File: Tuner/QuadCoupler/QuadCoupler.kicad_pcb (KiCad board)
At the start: 2 copper layers, 100 x 100 mm, 89 parts, among them J1 Conn_01x02, J10 Conn_01x02, J2 Conn_Coaxial, J21 Conn_01x01, J22 Conn_01x01, J23 Conn_01x01, J24 Conn_01x01, J3 Conn_Coaxial, J4 Conn_Coaxial, J5 Conn_Coaxial, J6 Conn_Coaxial, J7 Conn_01x02, J8 Conn_01x02, J9 Conn_01x02

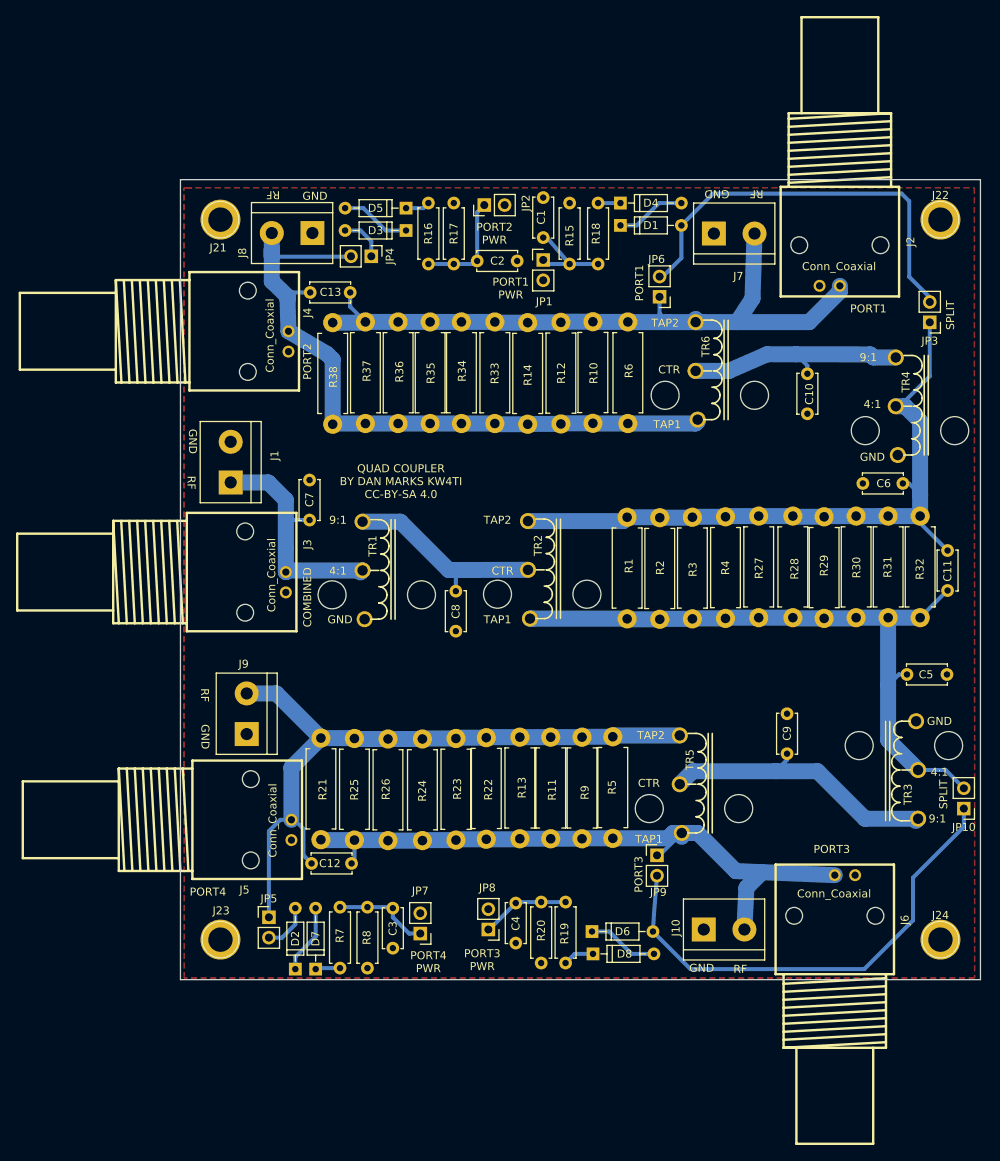
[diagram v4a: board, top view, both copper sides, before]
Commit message: Added BNC and screw terminal combo pads
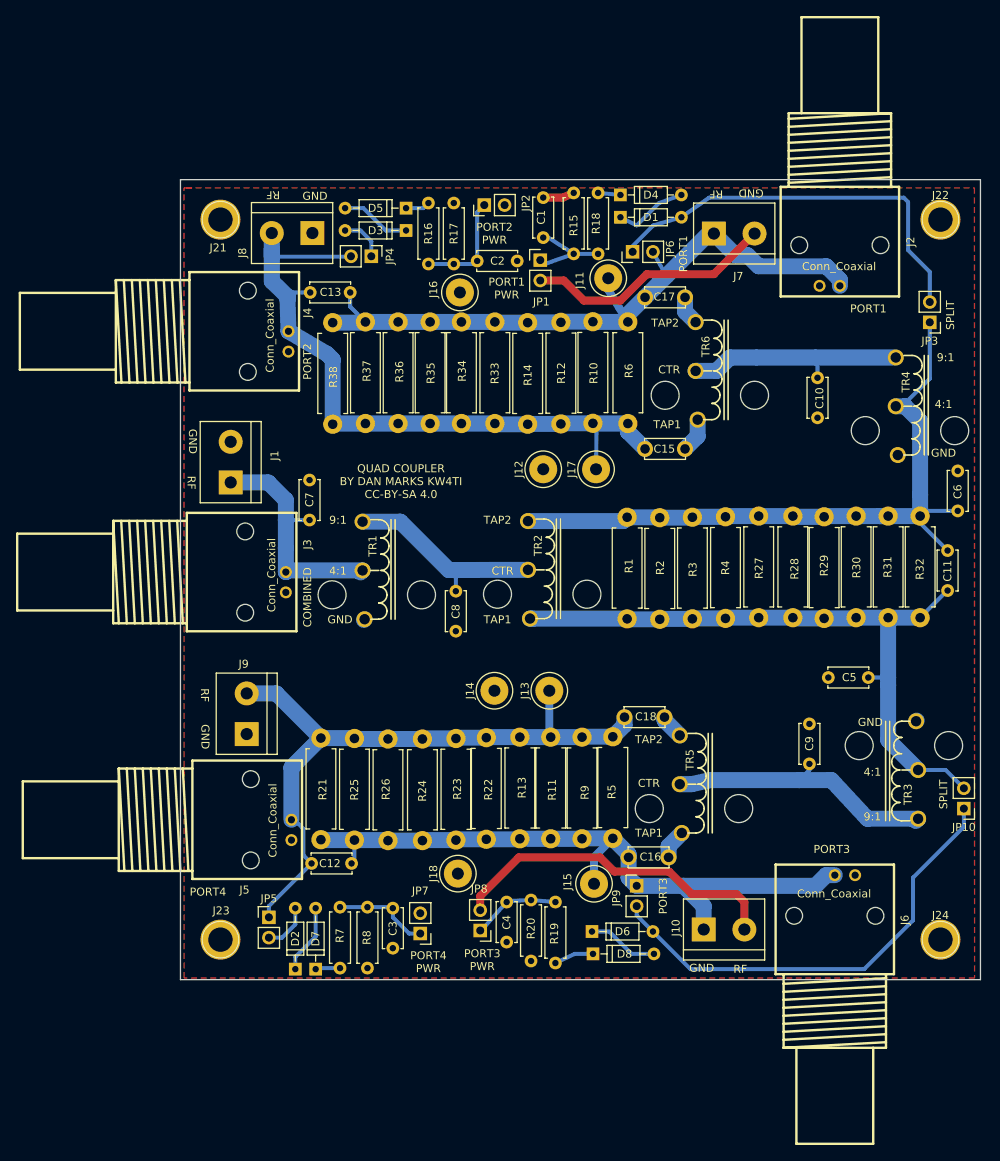
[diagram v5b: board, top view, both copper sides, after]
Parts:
- added C15: NC, Capacitors_THT:C_Disc_D5.0mm_W2.5mm_P5.00mm, F.Cu at (98.1, 73.7)
- added C16: NC, Capacitors_THT:C_Disc_D5.0mm_W2.5mm_P5.00mm, F.Cu at (96.0, 124.7)
- added C17: NC, Capacitors_THT:C_Disc_D5.0mm_W2.5mm_P5.00mm, F.Cu at (98.1, 54.7)
- added C18: NC, Capacitors_THT:C_Disc_D5.0mm_W2.5mm_P5.00mm, F.Cu at (95.5, 107.2)
- added J11: Conn_01x01, Connectors:1pin, F.Cu at (93.5, 52.3)
- added J12: Conn_01x01, Connectors:1pin, F.Cu at (85.3, 76.2)
- added J13: Conn_01x01, Connectors:1pin, F.Cu at (86.1, 103.9)
- added J14: Conn_01x01, Connectors:1pin, F.Cu at (79.2, 103.9)
- added J15: Conn_01x01, Connectors:1pin, F.Cu at (91.7, 128.0)
- added J16: Conn_01x01, Connectors:1pin, F.Cu at (74.9, 54.1)
- added J17: Conn_01x01, Connectors:1pin, F.Cu at (91.9, 76.2)
- added J18: Conn_01x01, Connectors:1pin, F.Cu at (74.7, 126.7)
- moved C6 7.67 mm to (137.2, 81.4), turned to 90 degrees
- moved JP6 6.56 mm to (96.5, 49.0), turned to 90 degrees
- moved C5 4.84 mm to (126.0, 102.2), turned to 180 degrees
- moved JP9 4.58 mm to (97.0, 128.3)
- moved C9 3.07 mm to (118.6, 113.0)
- moved R15 1.37 mm to (89.2, 41.7)
- moved C10 1.37 mm to (119.6, 64.8)
- moved R20 1.30 mm to (83.8, 137.7)
- moved R19 1.27 mm to (86.9, 130.3)
- moved R18 1.27 mm to (92.2, 49.3)
- moved C4 1.15 mm to (80.8, 130.3)
- moved JP8 1.02 mm to (77.5, 133.9)
- moved D4 1.02 mm to (95.0, 41.9)
- moved D1 1.02 mm to (95.0, 44.7)
- moved JP1 0.37 mm to (85.0, 50.1)
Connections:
- J10 pad 1: GND -> Net-(C12-Pad2)
- J10 pad 2: Net-(C12-Pad2) -> GND
- J7 pad 1: GND -> Net-(C13-Pad1)
- J7 pad 2: Net-(C13-Pad1) -> GND
- JP6 pad 1: Net-(C13-Pad1) -> Net-(D1-Pad2)
- JP6 pad 2: Net-(D1-Pad2) -> Net-(C13-Pad1)
- TR5 pad 1: Net-(C12-Pad2) -> Net-(C16-Pad2)
- TR5 pad 3: Net-(C12-Pad1) -> Net-(C18-Pad2)
- TR6 pad 1: Net-(C13-Pad2) -> Net-(C15-Pad2)
- TR6 pad 3: Net-(C13-Pad1) -> Net-(C17-Pad2)
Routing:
- net GND: track 0.54 -> 78.2 mm
- net Net-(C12-Pad1): track 89.4 -> 84.9 mm
- net Net-(C15-Pad2): track 0.00 -> 4.31 mm
- net Net-(C16-Pad2): track 0.00 -> 3.73 mm
- net Net-(C17-Pad2): track 0.00 -> 3.65 mm
- net Net-(C12-Pad2): track 82.4 -> 86.0 mm
- net Net-(C18-Pad2): track 0.00 -> 3.08 mm
- net Net-(D6-Pad2): track 60.6 -> 57.6 mm
- net Net-(C11-Pad1): track 89.4 -> 92.3 mm
- net Net-(C9-Pad1): track 36.1 -> 34.9 mm
- net Net-(D8-Pad1): track 3.90 -> 4.96 mm
- net Net-(C13-Pad2): track 88.8 -> 89.7 mm
- net Net-(C13-Pad1): track 87.0 -> 86.2 mm

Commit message: Changed over yet more to BNC
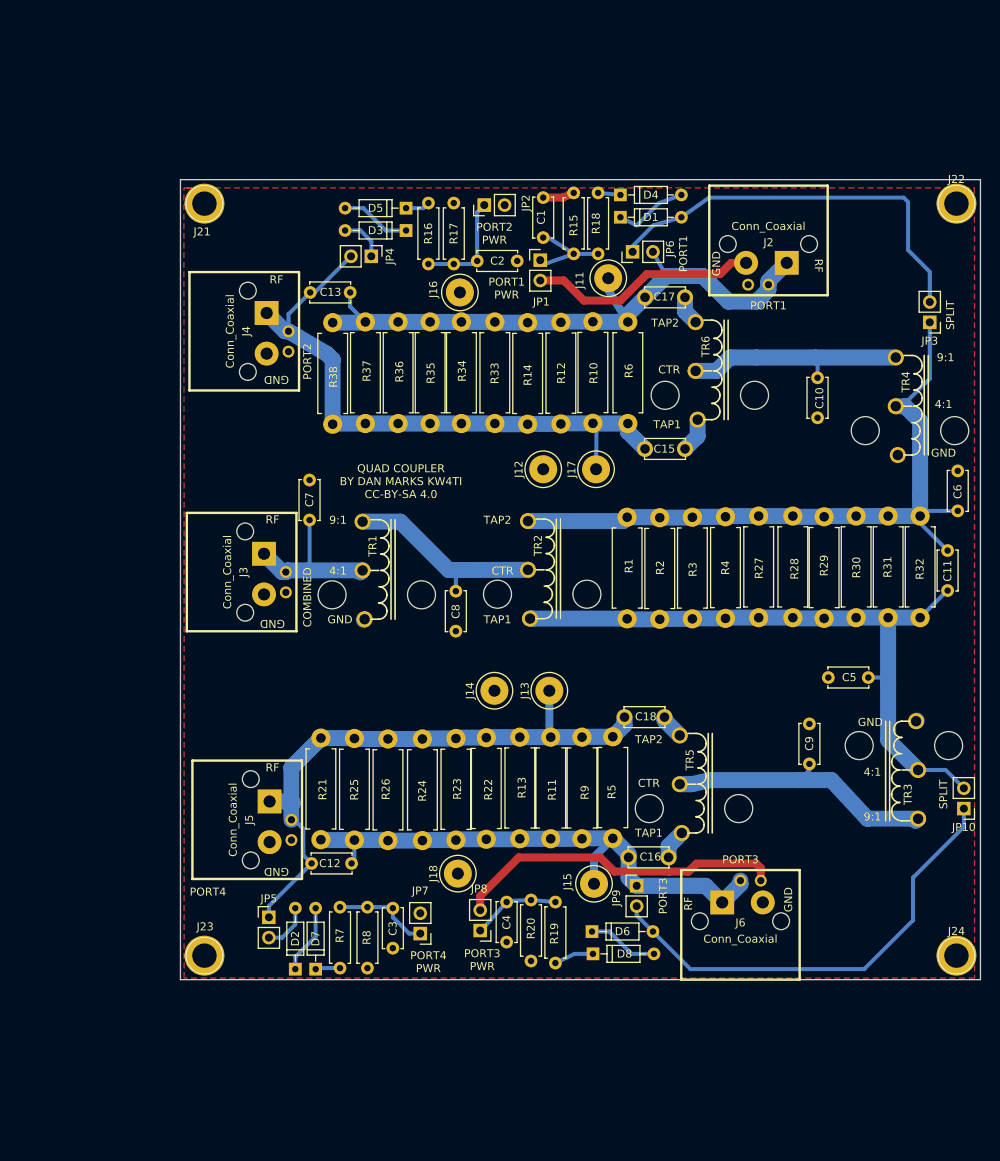
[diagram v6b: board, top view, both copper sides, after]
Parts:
- removed J1, J10, J7, J8, J9: Conn_01x02, Connectors_Terminal_Blocks:TerminalBlock_bornier-2_P5.08mm
- J2, J3, J4, J5, J6: footprint QuadCoupler:bnc_90_1-1337543-0 -> QuadCoupler:bnc_90_1-1337543-0_pad_combo
- moved J6 11.8 mm to (110.0, 140.0)
- moved J2 8.93 mm to (113.5, 40.8)
- moved J21 2.83 mm to (43.0, 43.0)
- moved J22 2.83 mm to (137.0, 43.0)
- moved J23 2.83 mm to (43.0, 137.0)
- moved J24 2.83 mm to (137.0, 137.0)
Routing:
- net Net-(C12-Pad2): track 86.0 -> 69.4 mm
- net Net-(C13-Pad2): track 89.7 -> 78.4 mm
- net Net-(C12-Pad1): track 84.9 -> 76.4 mm
- net Net-(C7-Pad1): track 30.6 -> 22.3 mm
- net Net-(C13-Pad1): track 86.2 -> 78.2 mm
- net GND: track 78.2 -> 74.7 mm

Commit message: TandenMatch now has DC-RF bias tee
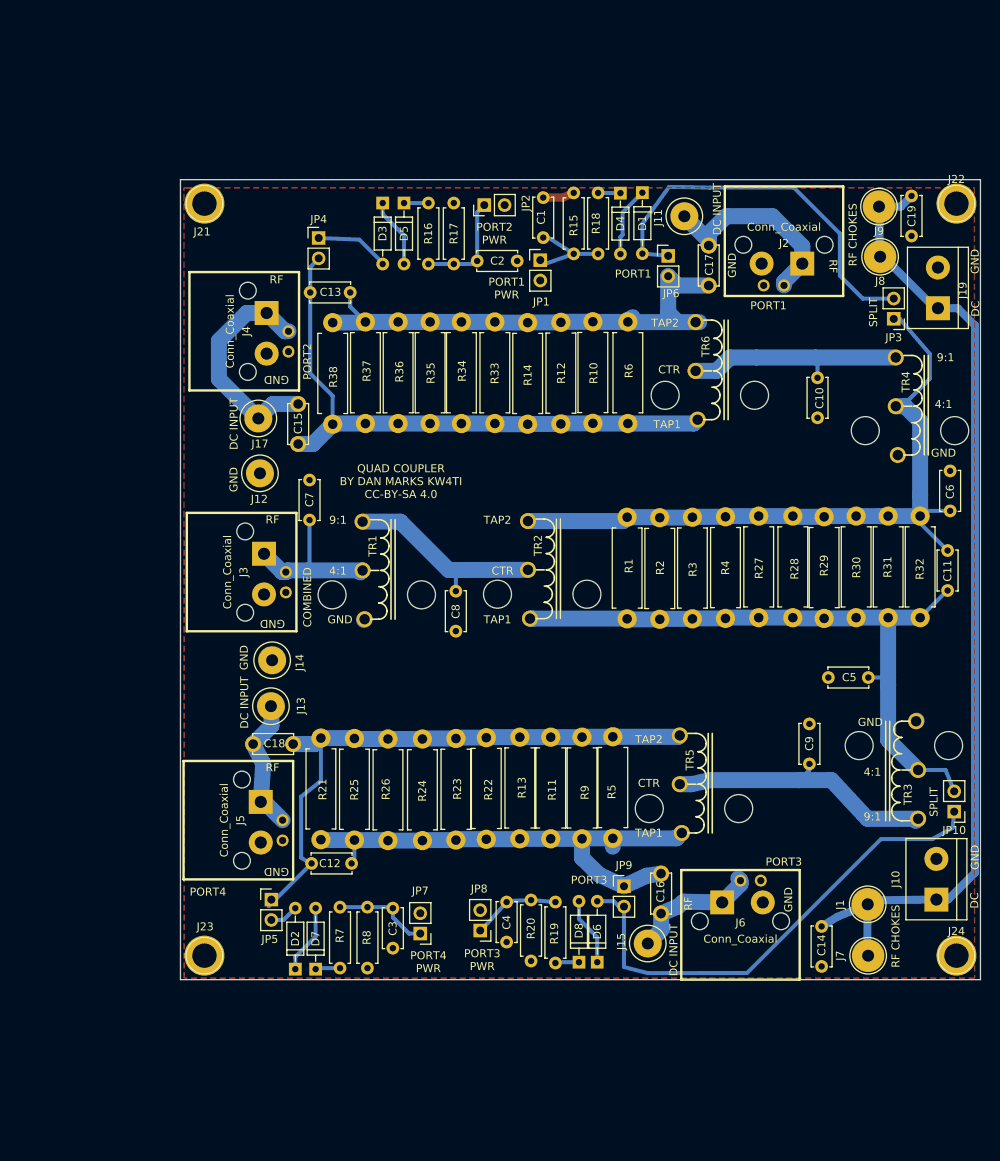
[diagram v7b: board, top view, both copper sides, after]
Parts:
- removed J16, J18: Conn_01x01, Connectors:1pin
- added C14: 10 nF, Capacitors_THT:C_Disc_D5.0mm_W2.5mm_P5.00mm, F.Cu at (120.1, 133.3)
- added C19: 10 nF, Capacitors_THT:C_Disc_D5.0mm_W2.5mm_P5.00mm, F.Cu at (131.4, 42.0)
- added J1: Conn_01x01, Connectors:1pin, F.Cu at (125.9, 130.6)
- added J10: Conn_01x02, Connectors_Terminal_Blocks:TerminalBlock_bornier-2_P5.08mm, F.Cu at (134.5, 130.0)
- added J19: Conn_01x02, Connectors_Terminal_Blocks:TerminalBlock_bornier-2_P5.08mm, F.Cu at (134.7, 56.1)
- added J7: Conn_01x01, Connectors:1pin, F.Cu at (126.0, 137.0)
- added J8: Conn_01x01, Connectors:1pin, F.Cu at (127.5, 49.6)
- added J9: Conn_01x01, Connectors:1pin, F.Cu at (127.3, 43.4)
- moved C18 46.5 mm to (49.1, 110.6)
- moved C15 43.7 mm to (54.7, 68.0), turned to 270 degrees
- moved J17 42.7 mm to (49.7, 69.8)
- moved J12 35.4 mm to (49.9, 76.7)
- moved J13 34.9 mm to (51.3, 105.8), turned to 0 degrees
- moved J14 28.0 mm to (51.5, 100.1), turned to 0 degrees
- moved J11 12.3 mm to (103.0, 44.6)
- moved C17 10.3 mm to (106.0, 48.2), turned to 270 degrees
- moved J15 10.0 mm to (98.4, 135.5)
- moved C16 8.12 mm to (100.1, 131.7), turned to 90 degrees
- moved JP4 6.96 mm to (57.3, 47.3), turned to 0 degrees
- moved JP3 4.53 mm to (129.2, 57.4)
- moved D3 4.50 mm to (65.3, 42.9), turned to 270 degrees
- moved JP6 4.47 mm to (101.0, 49.5), turned to 0 degrees
- moved D1 4.12 mm to (97.7, 41.6), turned to 270 degrees
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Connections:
- C15 pad 1: Net-(C13-Pad2) -> Net-(C15-Pad1)
- C15 pad 2: Net-(C15-Pad2) -> Net-(C13-Pad2)
- C16 pad 1: Net-(C12-Pad2) -> Net-(C16-Pad1)
- C16 pad 2: Net-(C16-Pad2) -> Net-(C12-Pad2)
- C17 pad 1: Net-(C13-Pad1) -> Net-(C17-Pad1)
- C17 pad 2: Net-(C17-Pad2) -> Net-(C13-Pad1)
- C18 pad 1: Net-(C12-Pad1) -> Net-(C18-Pad1)
- C18 pad 2: Net-(C18-Pad2) -> Net-(C12-Pad1)
- J11 pad 1: Net-(C13-Pad1) -> Net-(C17-Pad1)
- J13 pad 1: Net-(C12-Pad1) -> Net-(C18-Pad1)
- J15 pad 1: Net-(C12-Pad2) -> Net-(C16-Pad1)
- J17 pad 1: Net-(C13-Pad2) -> Net-(C15-Pad1)
- J2 pad 1: Net-(C13-Pad1) -> Net-(C17-Pad1)
- J4 pad 1: Net-(C13-Pad2) -> Net-(C15-Pad1)
- J5 pad 1: Net-(C12-Pad1) -> Net-(C18-Pad1)
- J6 pad 1: Net-(C12-Pad2) -> Net-(C16-Pad1)
- TR5 pad 1: Net-(C16-Pad2) -> Net-(C12-Pad2)
- TR5 pad 3: Net-(C18-Pad2) -> Net-(C12-Pad1)
- TR6 pad 1: Net-(C15-Pad2) -> Net-(C13-Pad2)
- TR6 pad 3: Net-(C17-Pad2) -> Net-(C13-Pad1)
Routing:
- net Net-(C14-Pad1): track 0.00 -> 122.4 mm
- net GND: track 74.7 -> 4.17 mm
- net Net-(C15-Pad1): track 0.00 -> 28.6 mm
- net Net-(C17-Pad1): track 0.00 -> 26.4 mm
- net Net-(C18-Pad1): track 0.00 -> 17.2 mm
- net Net-(C16-Pad1): track 0.00 -> 16.5 mm
- net Net-(C13-Pad1): track 78.2 -> 64.2 mm
- net Net-(C12-Pad2): track 69.4 -> 64.1 mm
- net Net-(C15-Pad2): track 4.31 -> 0.00 mm
- net Net-(D6-Pad2): track 57.6 -> 61.7 mm
- net Net-(C16-Pad2): track 3.73 -> 0.00 mm
- net Net-(C17-Pad2): track 3.65 -> 0.00 mm
- net Net-(D3-Pad2): track 5.71 -> 9.34 mm
- net Net-(C13-Pad2): track 78.4 -> 74.8 mm
- net Net-(C18-Pad2): track 3.08 -> 0.00 mm
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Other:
- board text added: "DC"
- board text added: "DC INPUT"
- board text added: "RF CHOKES"

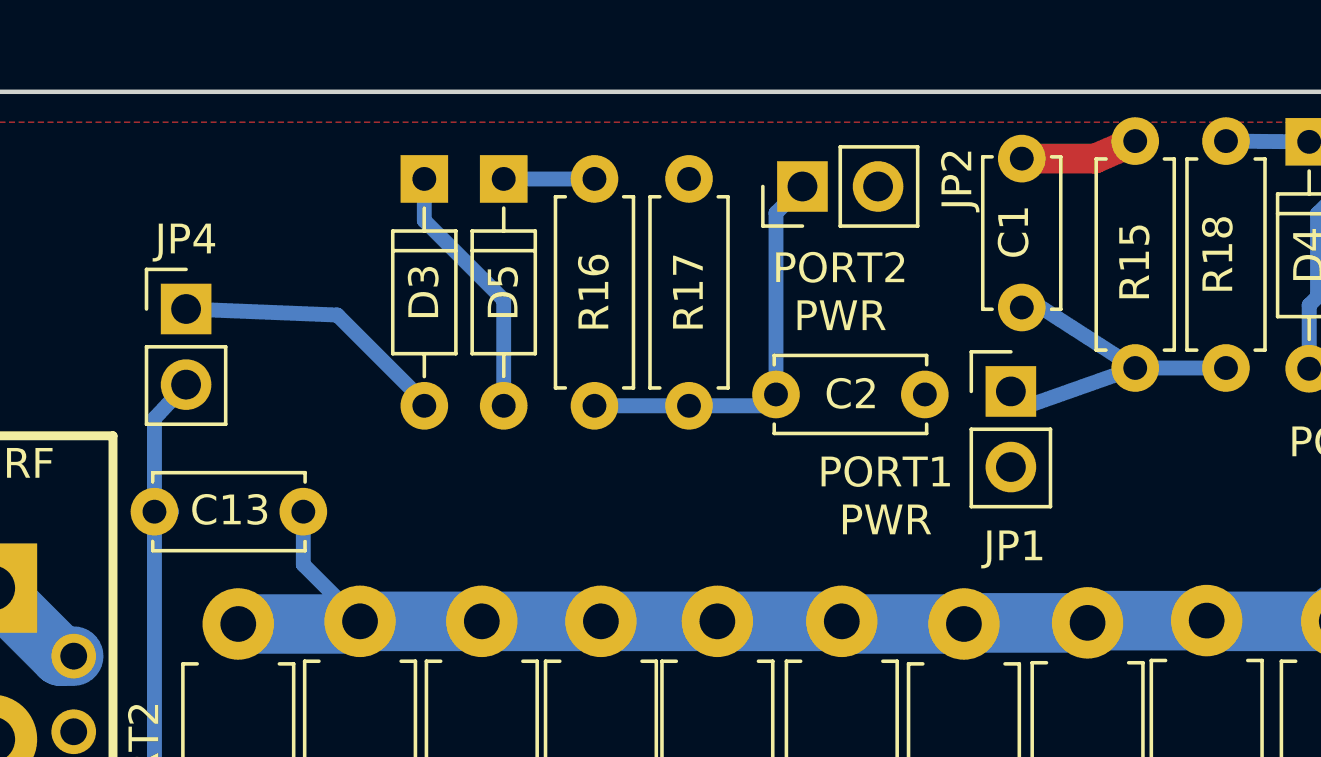
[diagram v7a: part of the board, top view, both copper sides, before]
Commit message: Symmetrized QuadCoupler Layout
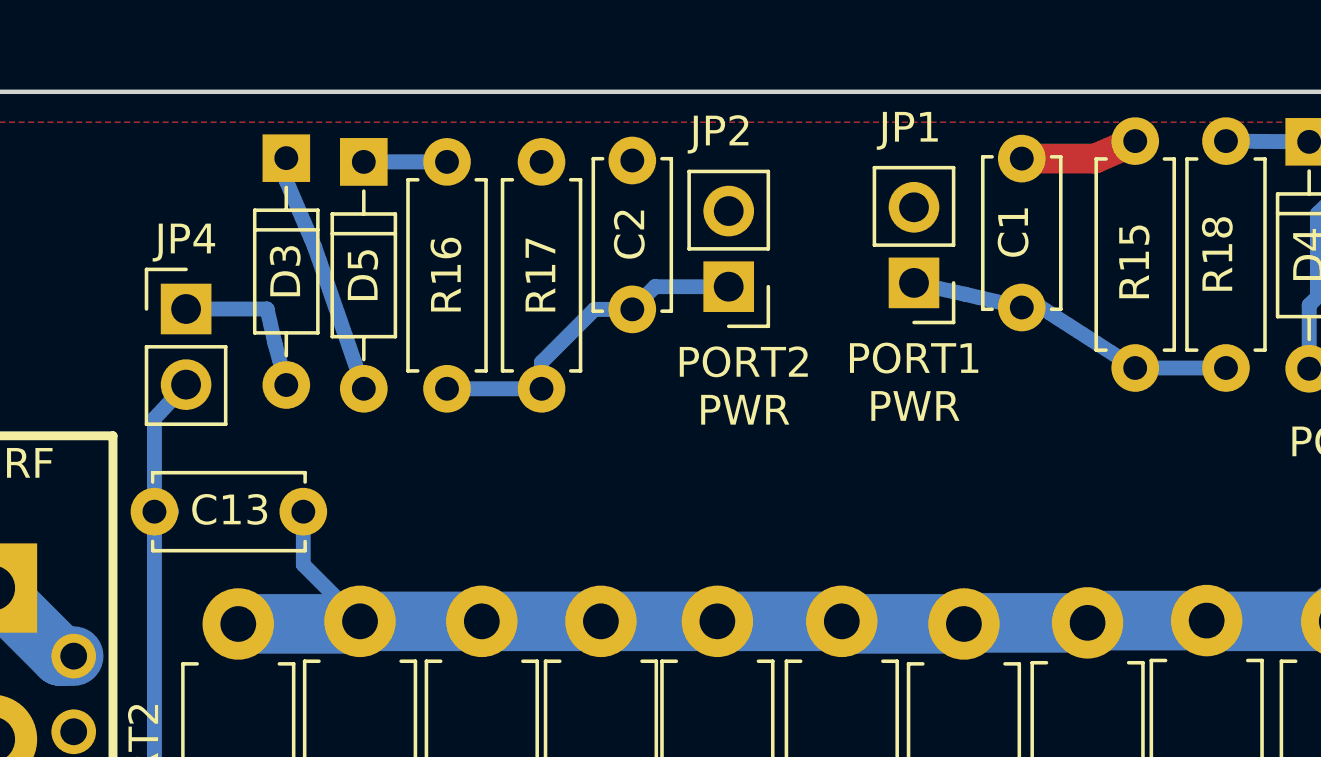
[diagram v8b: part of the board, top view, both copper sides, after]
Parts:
- moved C2 5.61 mm to (72.3, 47.3), turned to 90 degrees
- moved R17 4.99 mm to (69.2, 42.4)
- moved R16 4.99 mm to (66.0, 50.0)
- moved JP1 4.89 mm to (81.7, 46.4), turned to 180 degrees
- moved D5 4.73 mm to (63.2, 42.4)
- moved D3 4.69 mm to (60.6, 42.2)
- moved JP2 4.18 mm to (75.5, 46.5), turned to 180 degrees
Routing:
- net Net-(D3-Pad2): track 9.34 -> 5.48 mm
- net Net-(C2-Pad1): track 13.8 -> 11.6 mm
- net Net-(C1-Pad1): track 12.2 -> 11.3 mm
- net Net-(D3-Pad1): track 8.72 -> 8.22 mm
